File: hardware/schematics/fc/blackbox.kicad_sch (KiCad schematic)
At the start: 3 parts

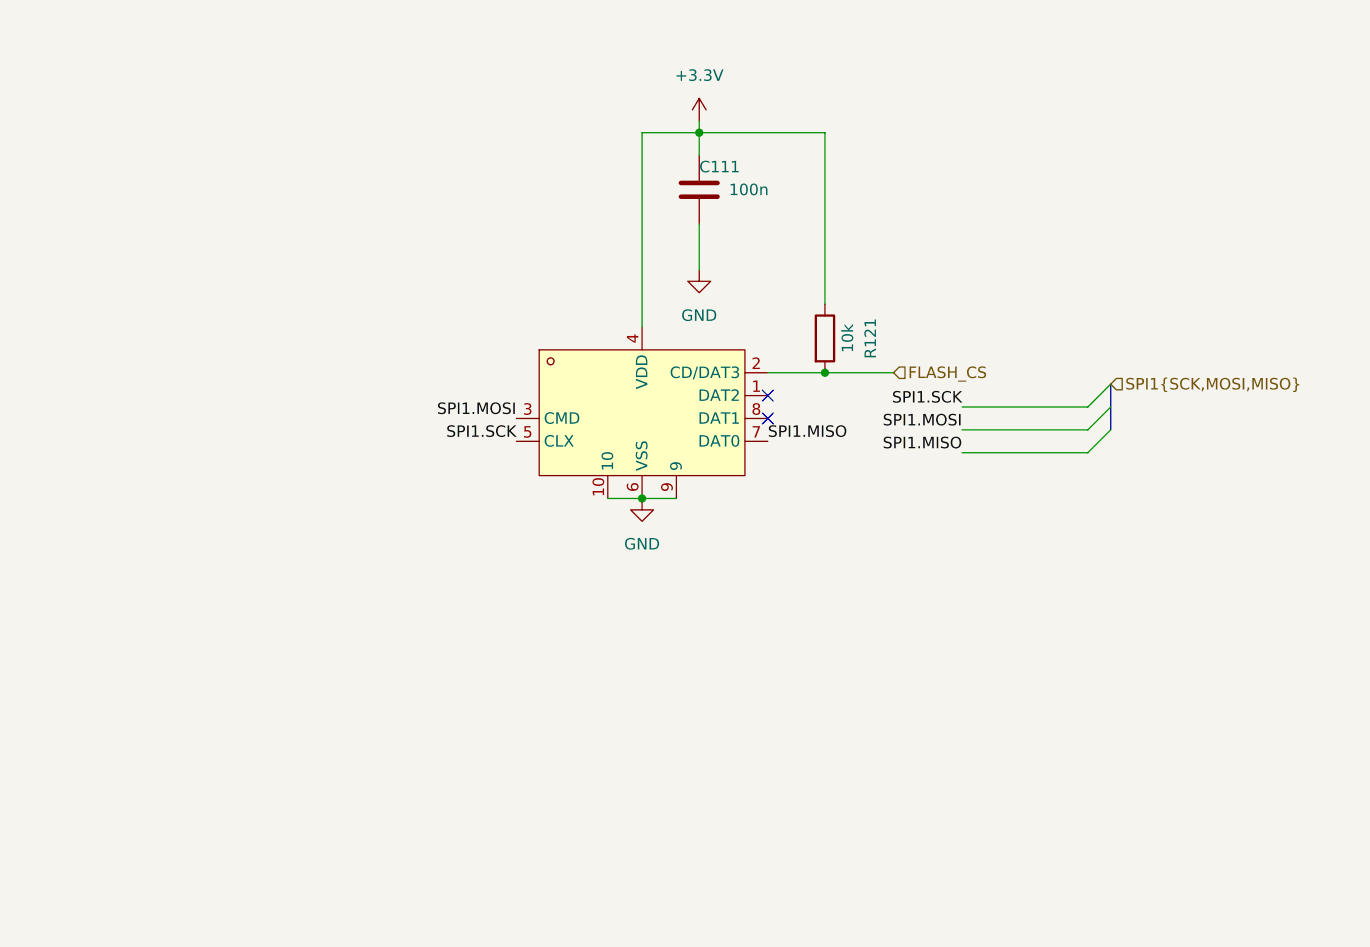
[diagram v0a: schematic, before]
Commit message: Whoop setup: restructure, import current FC/RX sheets, Bluejay libs, research docs
- KiCad project moved under hardware/ (family convention)
- FC sheets <- OpenFC-Lite-Mini rev2 (osd dropped: digital-only, root never
  referenced it); ELRS sheet <- OpenRX-Lite; orphaned esc_main deleted;
  esc_channel x4 kept as inherited placeholder pending Bluejay redraw
- Libraries replaced: lib (Lite-Mini), components/4in1ESC (4in1-mini donors),
  OpenRX-Shared (3D paths rewritten project-local via pcbnew API), new 'whoop'
  lib re-imported fresh via easyeda2kicad (EFM8BB51F16G, AGM310MAP, BY25Q64)
- sym-lib-table duplicate stale iCloud OpenRX-Shared entries fixed
- datasheets/ assembled (FC/ESC/ELRS); stale toothpick ESC docs removed
- docs/ESC_DESIGN.md extended with 2026-06 sourcing + market reality check
  (AGM310MAP thermal/supply limits, 12A class floor, BY25Q64 substitute)
- README/market research rewritten for digital-only Bluejay whoop scope
- Hierarchy verified via kicad-cli netlist export

Co-Authored-By: Claude Fable 5 <noreply@anthropic.com>
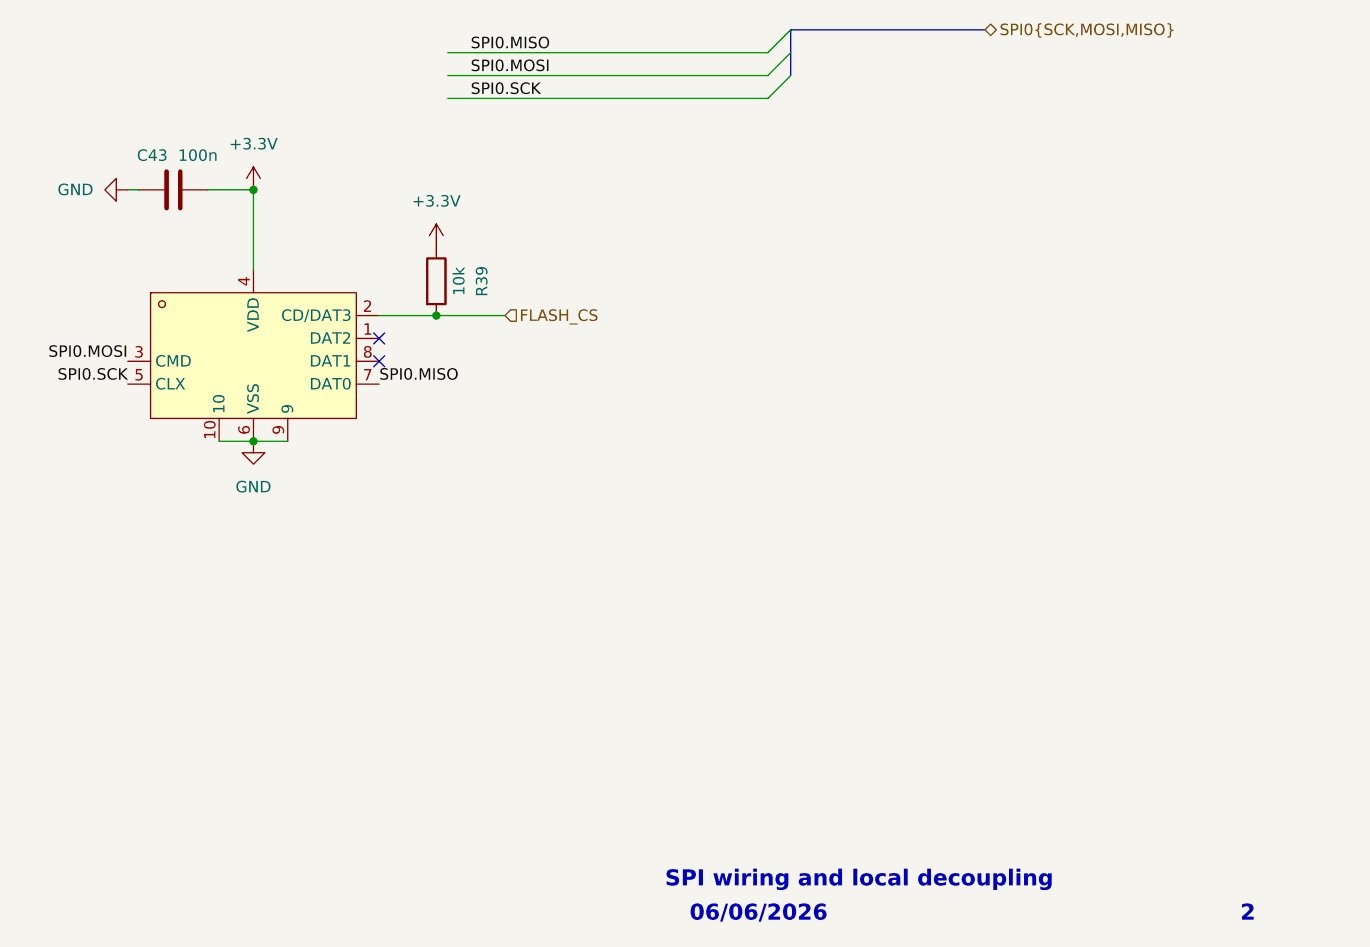
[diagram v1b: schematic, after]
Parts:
- renumbered C111 to C43, R121 to R39
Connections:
- net SPI1.MISO renamed SPI0.MISO
- net SPI1.MOSI renamed SPI0.MOSI
- net SPI1.SCK renamed SPI0.SCK
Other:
- note added: "06/06/2026"
- note added: "2"
- note added: "SPI wiring and local decoupling"
- moved on the sheet: C43, R39
